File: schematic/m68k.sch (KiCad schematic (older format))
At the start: 42 parts, among them J1 Power, J2 CONN_01X03, J3 JTAG, J4 CONN_02X30, J5 I2C, SW1 SW_Push_Dual, U1 M68SEC000, U10 MCP23008, U2 AS6C8016, U3 LM1084IT-3.3/NOPB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

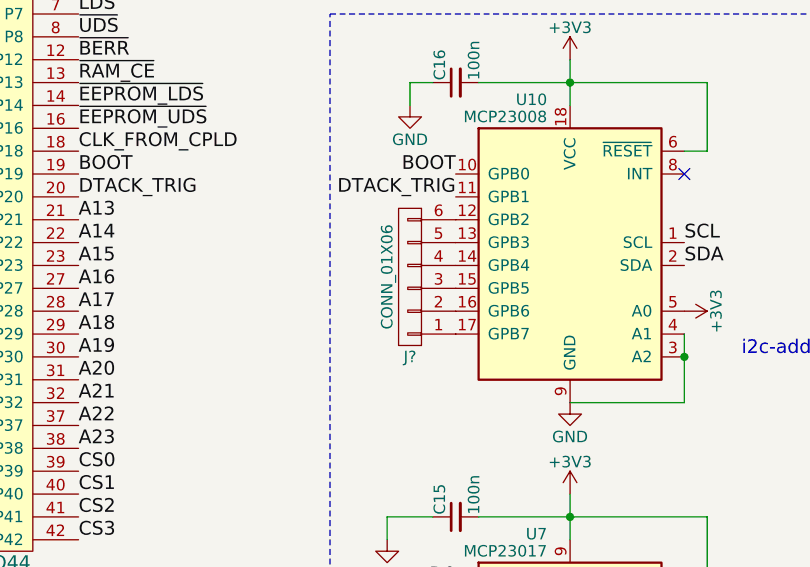
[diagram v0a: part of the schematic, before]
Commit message: - added halt_n and reset_n to 8-bit portexpander - implemented dtack state machine - some simple test benching
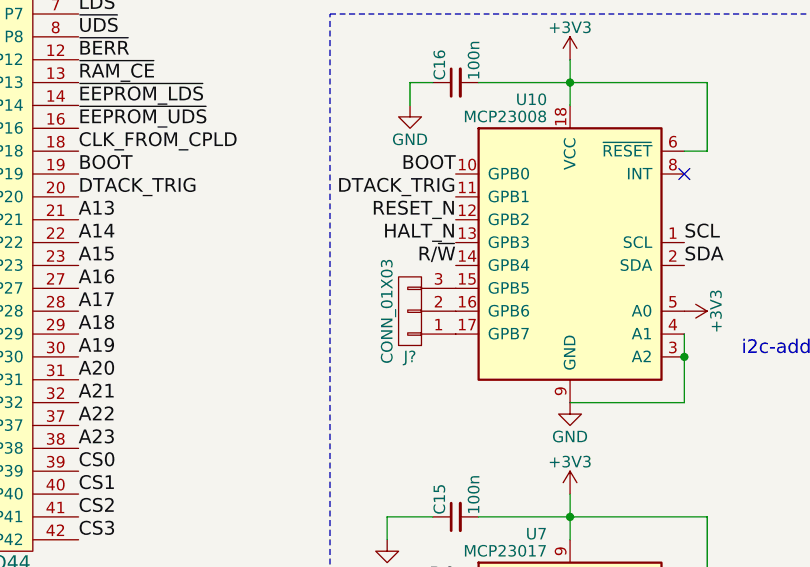
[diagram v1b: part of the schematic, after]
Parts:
- removed J?: CONN_01X06, symbol CONN_01X06
- added J?: CONN_01X03, symbol CONN_01X03
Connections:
- net R/~W: now also U10.14 (GPB4)
- net RESET_N: now reaches U10.12 (GPB2)
- net HALT_N: now reaches U10.13 (GPB3)
- net at U10.15 (GPB5): now also J?.3 (P3)
- net at U10.16 (GPB6): now also J?.2 (P2)
- net at U10.17 (GPB7): now also J?.1 (P1)
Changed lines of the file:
@@
-$EndComp
-$Comp
-L CONN_01X06 J?
-U 1 1 598F1D1B
-P 12300 2900
-F 0 "J?" H 12300 3250 50  0000 C CNN
-F 1 "CONN_01X06" V 12400 2900 50  0000 C CNN
-F 2 "" H 12300 2900 50  0001 C CNN
-F 3 "" H 12300 2900 50  0001 C CNN
-	1    12300 2900
-	-1   0    0    1
 $EndComp
 $Comp
@@
 Text Label 10550 7500 0    60   ~ 0
 CS3
+Text Label 12500 2650 2    60   ~ 0
+RESET_N
+Text Label 12500 2750 2    60   ~ 0
+HALT_N
+$Comp
+L CONN_01X03 J?
+U 1 1 599050EF
+P 12300 3050
+F 0 "J?" H 12300 3250 50  0000 C CNN
+F 1 "CONN_01X03" V 12400 3050 50  0000 C CNN
+F 2 "" H 12300 3050 50  0001 C CNN
+F 3 "" H 12300 3050 50  0001 C CNN
+	1    12300 3050
+	-1   0    0    1
+$EndComp
+Text Label 12500 2850 2    60   ~ 0
+R/~W
 $EndSCHEMATC

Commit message: layout start
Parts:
- removed J?: CONN_01X03, symbol CONN_01X03
- added J6, J8: CONN_02X30, Connectors:IDC_Header_Straight_60pins, symbol CONN_02X30
- added J7: CONN_01X02, Pin_Headers:Pin_Header_Straight_1x02, symbol CONN_01X02
- added R2: 100, Resistors_SMD:R_0805_HandSoldering, symbol R_Small
- J9: renamed from J?; footprint (none) -> Pin_Headers:Pin_Header_Straight_1x03_Pitch2.54mm
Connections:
- net HALT_N is gone; now on net ~HALT: U10.13 (GPB3)
- net RESET_N is gone; now on net ~RESET: U10.12 (GPB2)
- net +3V3: now also J6.4 (P4), J8.4 (P4)
- net +5V: now also J6.2 (P2), J8.2 (P2)
- net A1: now also J6.5 (P5), J8.5 (P5)
- net A10: now also J6.14 (P14), J8.14 (P14)
- net A11: now also J6.15 (P15), J8.15 (P15)
- net A12: now also J6.16 (P16), J8.16 (P16)
- net A13: now also J6.17 (P17), J8.17 (P17)
- net A14: now also J6.18 (P18), J8.18 (P18)
- net A15: now also J6.19 (P19), J8.19 (P19)
- net A16: now also J6.20 (P20), J8.20 (P20)
- net A17: now also J6.21 (P21), J8.21 (P21)
- net A18: now also J6.22 (P22), J8.22 (P22)
- net A19: now also J6.23 (P23), J8.23 (P23)
- net A2: now also J6.6 (P6), J8.6 (P6)
- net A20: now also J6.24 (P24), J8.24 (P24)
- net A21: now also J6.25 (P25), J8.25 (P25)
- net A22: now also J6.26 (P26), J8.26 (P26)
- net A23: now also J6.27 (P27), J8.27 (P27)
- net A3: now also J6.7 (P7), J8.7 (P7)
- net A4: now also J6.8 (P8), J8.8 (P8)
- net A5: now also J6.9 (P9), J8.9 (P9)
- net A6: now also J6.10 (P10), J8.10 (P10)
- net A7: now also J6.11 (P11), J8.11 (P11)
- net A8: now also J6.12 (P12), J8.12 (P12)
- net A9: now also J6.13 (P13), J8.13 (P13)
- net BOOT: now also J6.54 (P54), J8.54 (P54)
- net CS0: now also J6.55 (P55), J8.55 (P55)
- net CS1: now also J6.56 (P56), J8.56 (P56)
- net CS2: now also J6.57 (P57), J8.57 (P57)
- net CS3: now also J6.58 (P58), J8.58 (P58)
- net D0: now also J6.28 (P28), J8.28 (P28)
- net D1: now also J6.29 (P29), J8.29 (P29)
- net D10: now also J6.38 (P38), J8.38 (P38)
- net D11: now also J6.39 (P39), J8.39 (P39)
- net D12: now also J6.40 (P40), J8.40 (P40)
- net D13: now also J6.41 (P41), J8.41 (P41)
- net D14: now also J6.42 (P42), J8.42 (P42)
- net D15: now also J6.43 (P43), J8.43 (P43)
- net D2: now also J6.30 (P30), J8.30 (P30)
- net D3: now also J6.31 (P31), J8.31 (P31)
- net D4: now also J6.32 (P32), J8.32 (P32)
- net D5: now also J6.33 (P33), J8.33 (P33)
- net D6: now also J6.34 (P34), J8.34 (P34)
- net D7: now also J6.35 (P35), J8.35 (P35)
- net D8: now also J6.36 (P36), J8.36 (P36)
- net D9: now also J6.37 (P37), J8.37 (P37)
- net GND: now also J6.1 (P1), J6.3 (P3), J8.1 (P1), J8.3 (P3)
- net R/~W: now also J6.45 (P45), J8.45 (P45)
- net ~AVEC: now also RN1.7 (R6), J6.50 (P50), J8.50 (P50); no longer RN1.3 (R2)
- net ~BERR: now also RN1.8 (R7); no longer RN1.7 (R6)
- net ~BG: now also RN1.3 (R2), J6.49 (P49), J8.49 (P49); no longer RN1.11 (R10)
- net ~BR: now also RN1.4 (R3), J6.48 (P48), J8.48 (P48); no longer RN1.10 (R9)
- net ~DTACK: now also J6.44 (P44), J8.44 (P44)
- net ~HALT: now also RN1.5 (R4); no longer RN1.9 (R8)
- net ~IPL0: now also RN1.11 (R10), J6.51 (P51), J8.51 (P51); no longer RN1.6 (R5)
- net ~IPL1: now also RN1.10 (R9), J6.52 (P52), J8.52 (P52); no longer RN1.5 (R4)
- net ~IPL2: now also RN1.9 (R8), J6.53 (P53), J8.53 (P53); no longer RN1.4 (R3)
- net ~LDS: now also J6.46 (P46), J8.46 (P46)
- net ~RESET: now also RN1.6 (R5), R2.2; no longer RN1.8 (R7)
- net ~UDS: now also J6.47 (P47), J8.47 (P47)
- net at U6.33 (GSR): now also R2.1
- net at U6.34 (GTS2): now also J7.1 (P1)
- net at U6.36 (GTS1): now also J7.2 (P2)
- no-connect marks 10 -> 14
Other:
- moved on the sheet: J4, RN1

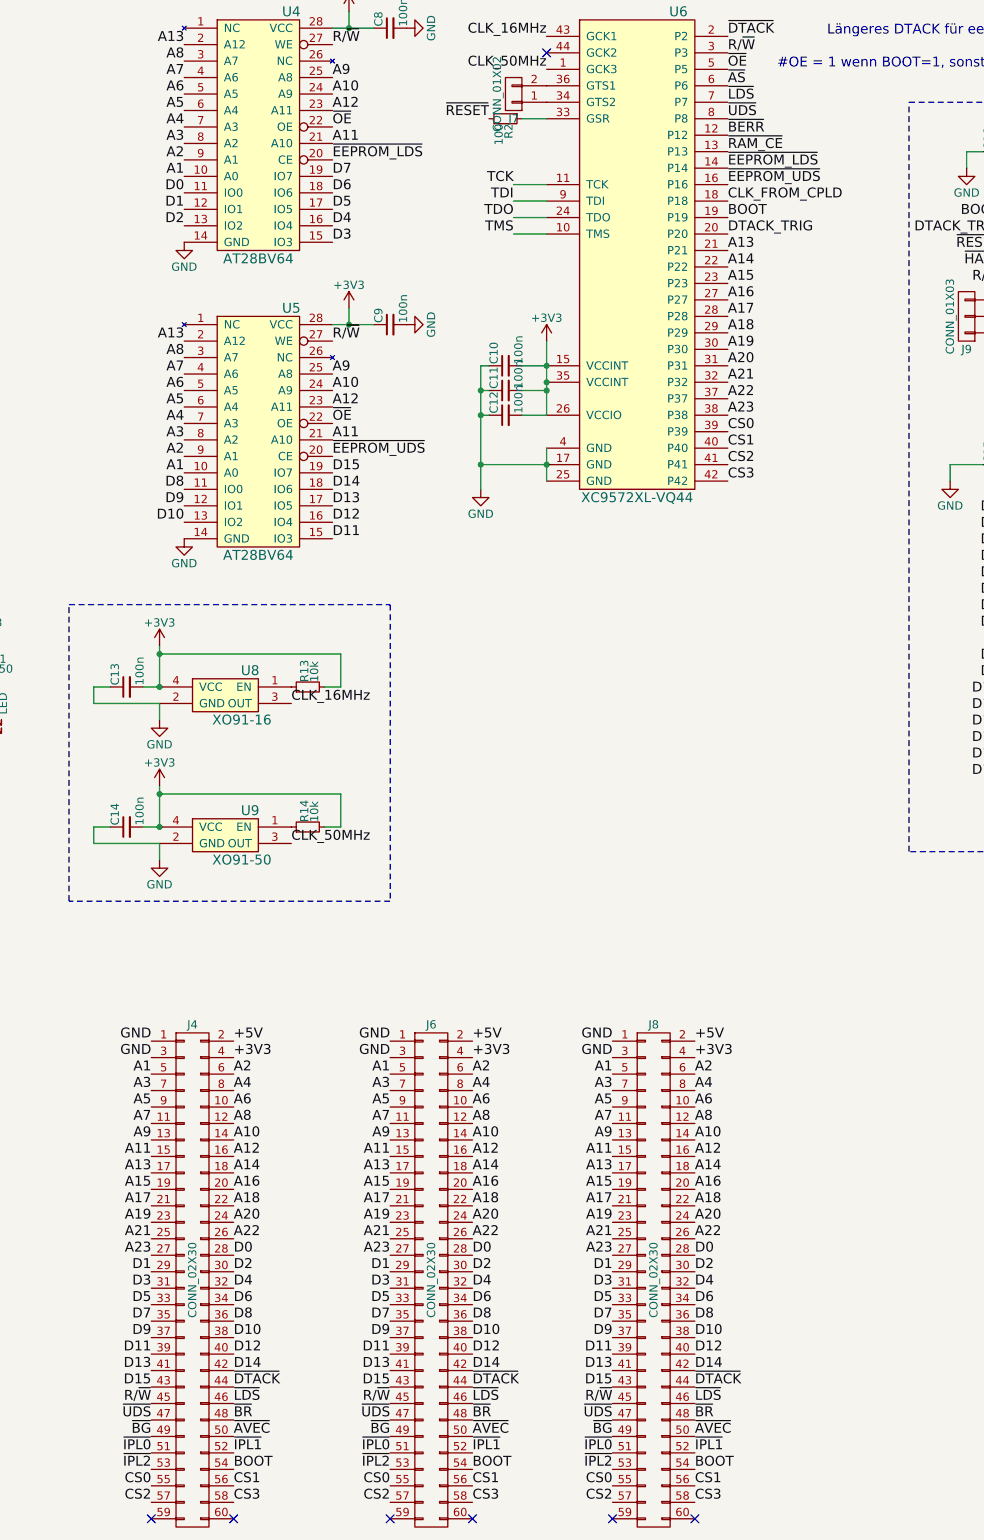
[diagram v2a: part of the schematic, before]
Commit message: - changed pin assignment - further layout
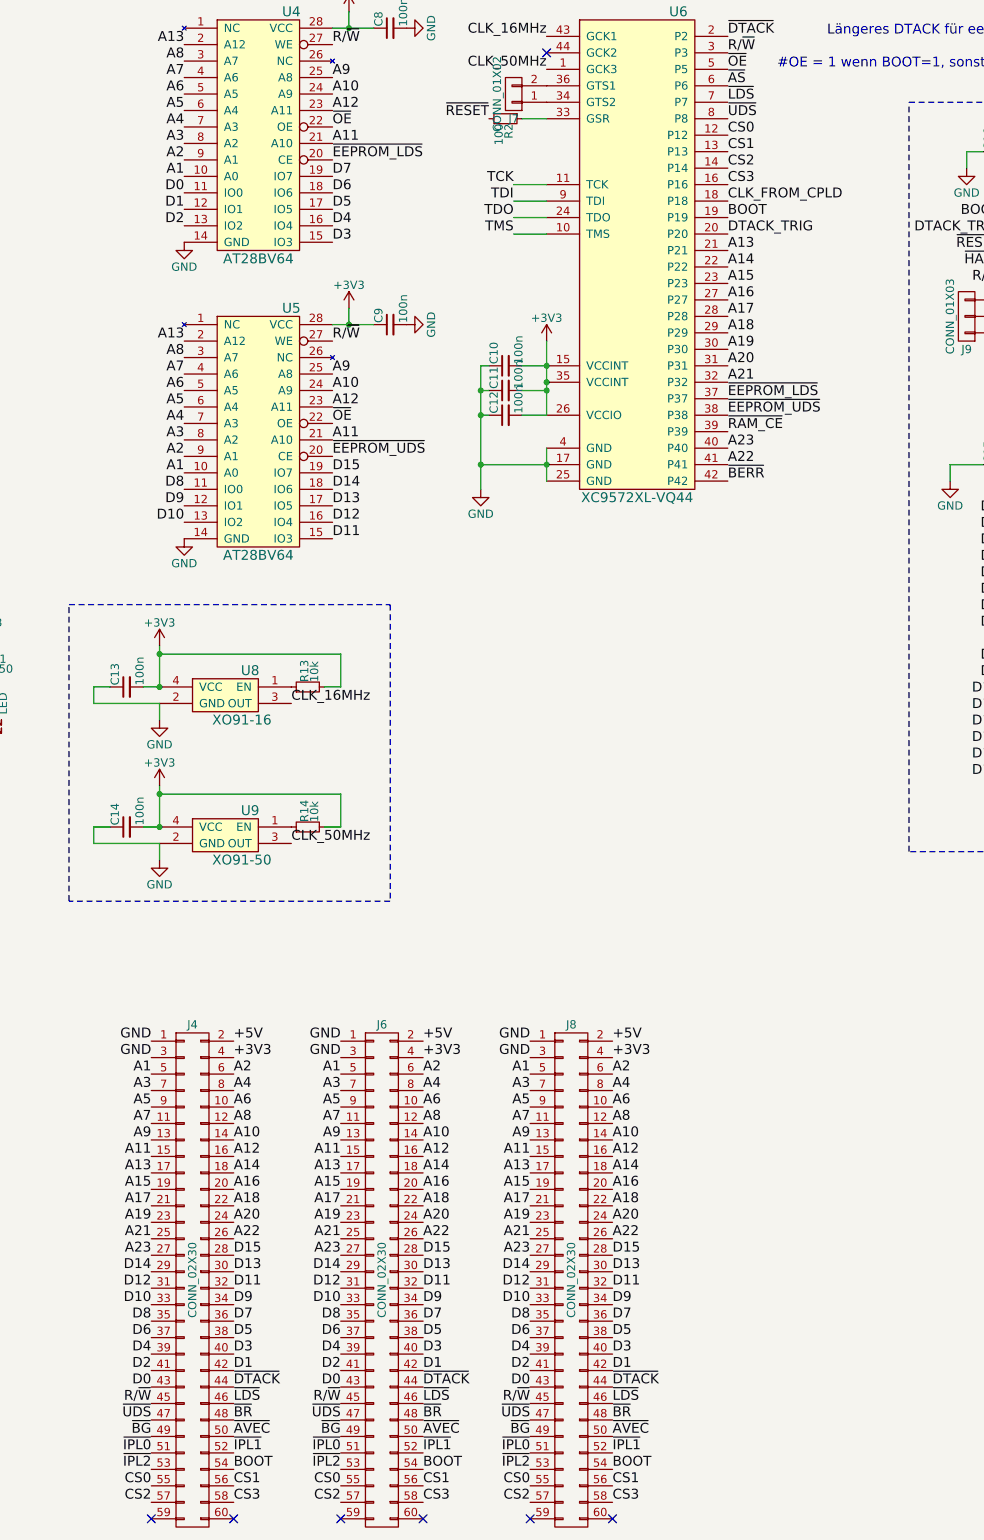
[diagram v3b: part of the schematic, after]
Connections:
- net A22: now also U6.41 (P41); no longer U6.37 (P37)
- net A23: now also U6.40 (P40); no longer U6.38 (P38)
- net CS0: now also U6.12 (P12); no longer U6.39 (P39)
- net CS1: now also U6.13 (P13); no longer U6.40 (P40)
- net CS2: now also U6.14 (P14); no longer U6.41 (P41)
- net CS3: now also U6.16 (P16); no longer U6.42 (P42)
- net D0: now also J4.43 (P43), J6.43 (P43), J8.43 (P43); no longer J4.28 (P28), J6.28 (P28), J8.28 (P28)
- net D1: now also J4.42 (P42), J6.42 (P42), J8.42 (P42); no longer J4.29 (P29), J6.29 (P29), J8.29 (P29)
- net D10: now also J4.33 (P33), J6.33 (P33), J8.33 (P33); no longer J4.38 (P38), J6.38 (P38), J8.38 (P38)
- net D11: now also J4.32 (P32), J6.32 (P32), J8.32 (P32); no longer J4.39 (P39), J6.39 (P39), J8.39 (P39)
- net D12: now also J4.31 (P31), J6.31 (P31), J8.31 (P31); no longer J4.40 (P40), J6.40 (P40), J8.40 (P40)
- net D13: now also J4.30 (P30), J6.30 (P30), J8.30 (P30); no longer J4.41 (P41), J6.41 (P41), J8.41 (P41)
- net D14: now also J4.29 (P29), J6.29 (P29), J8.29 (P29); no longer J4.42 (P42), J6.42 (P42), J8.42 (P42)
- net D15: now also J4.28 (P28), J6.28 (P28), J8.28 (P28); no longer J4.43 (P43), J6.43 (P43), J8.43 (P43)
- net D2: now also J4.41 (P41), J6.41 (P41), J8.41 (P41); no longer J4.30 (P30), J6.30 (P30), J8.30 (P30)
- net D3: now also J4.40 (P40), J6.40 (P40), J8.40 (P40); no longer J4.31 (P31), J6.31 (P31), J8.31 (P31)
- net D4: now also J4.39 (P39), J6.39 (P39), J8.39 (P39); no longer J4.32 (P32), J6.32 (P32), J8.32 (P32)
- net D5: now also J4.38 (P38), J6.38 (P38), J8.38 (P38); no longer J4.33 (P33), J6.33 (P33), J8.33 (P33)
- net D6: now also J4.37 (P37), J6.37 (P37), J8.37 (P37); no longer J4.34 (P34), J6.34 (P34), J8.34 (P34)
- net D7: now also J4.36 (P36), J6.36 (P36), J8.36 (P36); no longer J4.35 (P35), J6.35 (P35), J8.35 (P35)
- net D8: now also J4.35 (P35), J6.35 (P35), J8.35 (P35); no longer J4.36 (P36), J6.36 (P36), J8.36 (P36)
- net D9: now also J4.34 (P34), J6.34 (P34), J8.34 (P34); no longer J4.37 (P37), J6.37 (P37), J8.37 (P37)
- net ~BERR: now also U6.42 (P42); no longer U6.12 (P12)
- net ~EEPROM_LDS: now also U6.37 (P37); no longer U6.14 (P14)
- net ~EEPROM_UDS: now also U6.38 (P38); no longer U6.16 (P16)
- net ~RAM_CE: now also U6.39 (P39); no longer U6.13 (P13)

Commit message: layout done
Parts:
- J1: symbol CONN_01X04 -> Conn_01X04
- J2, J5, J9: symbol CONN_01X03 -> Conn_01X03
- J3: symbol CONN_01X06 -> Conn_01X06
- J4, J6, J8: symbol CONN_02X30 -> Conn_02X30
- J7: symbol CONN_01X02 -> Conn_01X02
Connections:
- no-connect marks 14 -> 17
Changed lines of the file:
@@
 EESchema Schematic File Version 2
+LIBS:m68k-rescue
 LIBS:power
 LIBS:device
@@
 LIBS:switches
 LIBS:m68k-cache
-EELAYER 25 0
+EELAYER 26 0
 EELAYER END
 $Descr A3 16535 11693
@@
 CLK_50MHz
 $Comp
-L CONN_01X06 J3
+L Conn_01X06 J3
 U 1 1 59881DD2
 P 4850 6750
@@
 $EndComp
 $Comp
-L CONN_01X03 J2
+L Conn_01X03 J2
 U 1 1 59883D86
 P 6150 6850
@@
 $EndComp
 $Comp
-L CONN_01X04 J1
+L Conn_01X04 J1
 U 1 1 5989E226
 P 3850 6850
@@
 Text Label 7350 10050 2    60   ~ 0
 ~IPL2
-Text Label 7850 10050 0    60   ~ 0
-BOOT
 $Comp
 L AS6C8016 U2
@@
 NoConn ~ 3250 1400
 $Comp
-L CONN_01X03 J5
+L Conn_01X03 J5
 U 1 1 598BE077
 P 2750 6800
@@
 Connection ~ 1950 6800
 $Comp
-L CONN_02X30 J4
+L Conn_02X30 J4
 U 1 1 598BF124
 P 7600 8900
@@
 ~HALT
 $Comp
-L CONN_01X03 J9
+L Conn_01X03 J9
 U 1 1 599050EF
 P 12300 3050
@@
 ~RESET
 $Comp
-L CONN_01X02 J7
+L Conn_01X02 J7
 U 1 1 59934E94
 P 9550 1700
@@
 Text Label 8500 10050 2    60   ~ 0
 ~IPL2
-Text Label 9000 10050 0    60   ~ 0
-BOOT
-$Comp
-L CONN_02X30 J6
+$Comp
+L Conn_02X30 J6
 U 1 1 5997FD38
 P 8750 8900
@@
 Text Label 9650 10050 2    60   ~ 0
 ~IPL2
-Text Label 10150 10050 0    60   ~ 0
-BOOT
-$Comp
-L CONN_02X30 J8
+$Comp
+L Conn_02X30 J8
 U 1 1 5997FDC7
 P 9900 8900
@@
 Text Label 10150 10250 0    60   ~ 0
 CS3
+NoConn ~ 10150 10050
+NoConn ~ 9000 10050
+NoConn ~ 7850 10050
 $EndSCHEMATC

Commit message: corrected footprints
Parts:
- J1: symbol Conn_01X04 -> CONN_01X04
- J2, J5, J9: symbol Conn_01X03 -> CONN_01X03
- J3: symbol Conn_01X06 -> CONN_01X06
- J4, J6, J8: symbol Conn_02X30 -> CONN_02X30
- J7: footprint Pin_Headers:Pin_Header_Straight_1x02 -> Pin_Headers:Pin_Header_Straight_1x02_Pitch2.54mm; symbol Conn_01X02 -> CONN_01X02
- U3: footprint TO_SOT_Packages_THT:TO-220_Vertical -> TO_SOT_Packages_THT:TO-220_Horizontal
- U4, U5, U7: footprint SMD_Packages:SOIC-28 -> Housings_SOIC:SOIC-28W_7.5x17.9mm_Pitch1.27mm
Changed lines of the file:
@@
 LIBS:switches
 LIBS:m68k-cache
-EELAYER 26 0
+EELAYER 25 0
 EELAYER END
 $Descr A3 16535 11693
@@
 CLK_50MHz
 $Comp
-L Conn_01X06 J3
+L CONN_01X06 J3
 U 1 1 59881DD2
 P 4850 6750
@@
 $EndComp
 $Comp
-L Conn_01X03 J2
+L CONN_01X03 J2
 U 1 1 59883D86
 P 6150 6850
@@
 F 0 "U4" H 8200 2600 60  0000 C CNN
 F 1 "AT28BV64" H 8000 1100 60  0000 C CNN
-F 2 "SMD_Packages:SOIC-28" H 7950 1250 60  0001 C CNN
+F 2 "Housings_SOIC:SOIC-28W_7.5x17.9mm_Pitch1.27mm" H 7950 1250 60  0001 C CNN
 F 3 "" H 7950 1250 60  0001 C CNN
 	1    8000 1900
@@
 F 0 "U5" H 8200 4400 60  0000 C CNN
 F 1 "AT28BV64" H 8000 2900 60  0000 C CNN
-F 2 "SMD_Packages:SOIC-28" H 7950 3050 60  0001 C CNN
+F 2 "Housings_SOIC:SOIC-28W_7.5x17.9mm_Pitch1.27mm" H 7950 3050 60  0001 C CNN
 F 3 "" H 7950 3050 60  0001 C CNN
 	1    8000 3700
@@
 F 0 "U3" H 5100 4600 50  0000 C CNN
 F 1 "LM1084IT-3.3/NOPB" H 4600 5000 50  0000 L CNN
-F 2 "TO_SOT_Packages_THT:TO-220_Vertical" H 4900 4900 50  0001 C CIN
+F 2 "TO_SOT_Packages_THT:TO-220_Horizontal" H 4900 4900 50  0001 C CIN
 F 3 "" H 4900 4800 50  0001 C CNN
 	1    4900 4800
@@
 $EndComp
 $Comp
-L Conn_01X04 J1
+L CONN_01X04 J1
 U 1 1 5989E226
 P 3850 6850
@@
 F 0 "U7" H 12900 6075 50  0000 R CNN
 F 1 "MCP23017" H 12900 6000 50  0000 R CNN
-F 2 "SMD_Packages:SOIC-28" H 13050 4100 50  0001 L CNN
+F 2 "Housings_SOIC:SOIC-28W_7.5x17.9mm_Pitch1.27mm" H 13050 4100 50  0001 L CNN
 F 3 "" H 13250 6050 50  0001 C CNN
 	1    13000 5050
@@
 NoConn ~ 3250 1400
 $Comp
-L Conn_01X03 J5
+L CONN_01X03 J5
 U 1 1 598BE077
 P 2750 6800
@@
 Connection ~ 1950 6800
 $Comp
-L Conn_02X30 J4
+L CONN_02X30 J4
 U 1 1 598BF124
 P 7600 8900
@@
 ~HALT
 $Comp
-L Conn_01X03 J9
+L CONN_01X03 J9
 U 1 1 599050EF
 P 12300 3050
@@
 ~RESET
 $Comp
-L Conn_01X02 J7
+L CONN_01X02 J7
 U 1 1 59934E94
 P 9550 1700
 F 0 "J7" H 9550 1850 50  0000 C CNN
 F 1 "CONN_01X02" V 9650 1700 50  0000 C CNN
-F 2 "Pin_Headers:Pin_Header_Straight_1x02" H 9550 1700 50  0001 C CNN
+F 2 "Pin_Headers:Pin_Header_Straight_1x02_Pitch2.54mm" H 9550 1700 50  0001 C CNN
 F 3 "" H 9550 1700 50  0001 C CNN
 	1    9550 1700
@@
 ~IPL2
 $Comp
-L Conn_02X30 J6
+L CONN_02X30 J6
 U 1 1 5997FD38
 P 8750 8900
@@
 ~IPL2
 $Comp
-L Conn_02X30 J8
+L CONN_02X30 J8
 U 1 1 5997FDC7
 P 9900 8900
